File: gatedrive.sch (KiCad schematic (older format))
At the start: 20 parts, among them IC1 HCPL-316J, IC2 IXDD614PI, p1 POWER SUPPLY CONNECTOR., p2 IGBT CONNECTOR., p3 CONTROLLER CONNECTOR.

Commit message: START
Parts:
- p1: value POWER SUPPLY CONNECTOR. -> SMPS CONNECTOR.
- p3: value CONTROLLER CONNECTOR. -> MIC CONNECTOR.
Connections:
- wire segments 48 -> 57
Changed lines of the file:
@@
 P 850 5100
 F 0 "p1" H 850 4900 50  0000 C CNN
-F 1 "POWER SUPPLY CONNECTOR." V 950 5100 39  0000 C CNN
+F 1 "SMPS CONNECTOR." V 950 5100 39  0000 C CNN
 F 2 "Terminal_Blocks:TerminalBlock_Pheonix_MKDS1.5-3pol" H 850 5100 50  0001 C CNN
 F 3 "" H 850 5100 50  0000 C CNN
@@
 P 850 6150
 F 0 "p3" H 850 5850 50  0000 C CNN
-F 1 "CONTROLLER CONNECTOR." V 950 6150 50  0000 C CNN
+F 1 "MIC CONNECTOR." V 950 6150 50  0000 C CNN
 F 2 "Socket_Strips:Socket_Strip_Straight_1x05" H 850 6150 50  0001 C CNN
 F 3 "" H 850 6150 50  0000 C CNN
@@
 a cap to ensure soft turn-off, recommended by datasheet of hcpl.
 Wire Wire Line
-	6950 4950 7500 4950
-Wire Wire Line
-	6250 4950 6650 4950
-Wire Wire Line
-	6250 5050 6250 5150
-Wire Wire Line
-	6250 4750 6250 4850
+	6950 4950 7150 4950
+Wire Wire Line
+	7150 4950 7500 4950
+Wire Wire Line
+	6250 4950 6500 4950
+Wire Wire Line
+	6500 4950 6650 4950
+Wire Wire Line
+	6250 5050 6250 5100
+Wire Wire Line
+	6250 5100 6250 5150
+Wire Wire Line
+	6250 4750 6250 4800
+Wire Wire Line
+	6250 4800 6250 4850
 Connection ~ 6550 4100
 Wire Wire Line
@@
 	6550 4100 6750 4100
 Wire Wire Line
-	6550 4050 6550 4650
+	6550 4050 6550 4100
+Wire Wire Line
+	6550 4100 6550 4650
 Connection ~ 8450 4950
 Wire Wire Line
@@
 Connection ~ 7150 4950
 Wire Wire Line
-	3700 4650 4850 4650
-Wire Wire Line
-	8350 4950 9050 4950
+	3700 4650 4000 4650
+Wire Wire Line
+	4000 4650 4850 4650
+Wire Wire Line
+	8350 4950 8450 4950
+Wire Wire Line
+	8450 4950 8900 4950
+Wire Wire Line
+	8900 4950 9050 4950
 Wire Wire Line
 	9350 4950 9450 4950
 Wire Wire Line
-	9750 4950 10200 4950
+	9750 4950 9950 4950
+Wire Wire Line
+	9950 4950 10200 4950
 Wire Wire Line
 	9700 5250 9950 5250
@@
 Wire Wire Line
 	7050 4100 7200 4100
-Text GLabel 1400 3100 0    60   Input ~ 0
+Text GLabel 1475 3050 0    60   Input ~ 0
 ~RST
 $Comp
 L PWR_FLAG #FLG07
 U 1 1 56C3962F
-P 1400 3100
-F 0 "#FLG07" H 1400 3195 50  0001 C CNN
-F 1 "PWR_FLAG" V 1550 3100 50  0000 C CNN
-F 2 "" H 1400 3100 50  0000 C CNN
-F 3 "" H 1400 3100 50  0000 C CNN
-	1    1400 3100
+P 1475 3050
+F 0 "#FLG07" H 1475 3145 50  0001 C CNN
+F 1 "PWR_FLAG" V 1625 3050 50  0000 C CNN
+F 2 "" H 1475 3050 50  0000 C CNN
+F 3 "" H 1475 3050 50  0000 C CNN
+	1    1475 3050
 	0    1    1    0
 $EndComp

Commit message: cleaning the repo
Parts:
- removed C1, C2, C4, C5: 0.1uF, Capacitors_ThroughHole:C_Disc_D3_P2.5, symbol CP1
- removed C3: 330pF, Capacitors_ThroughHole:C_Disc_D3_P2.5, symbol CP1
- removed C6: 100pF, Capacitors_ThroughHole:C_Disc_D3_P2.5, symbol CP1
- removed C7: 10nF, Capacitors_ThroughHole:C_Disc_D3_P2.5, symbol CP1
- removed D1: RGPO2-20, Diodes_ThroughHole:Diode_DO-41_SOD81_Horizontal_RM10, symbol D
- removed D2: 1N5821, Diodes_ThroughHole:Diode_DO-41_SOD81_Horizontal_RM10, symbol D
- removed IC1: HCPL-316J, Housings_SOIC:SOIC-16_7.5x10.3mm_Pitch1.27mm, symbol HCPL-316J-RESCUE-gatedrive
- removed IC2: IXDD614PI, gatedrive:DIP-8_W7.62mm_LongPads, symbol IXDD614PI-RESCUE-gatedrive
- removed R1: 10K, Capacitors_SMD:C_1206_HandSoldering, symbol R
- removed R2: 25K, Capacitors_SMD:C_1206_HandSoldering, symbol R
- removed R3, R6: 100, Capacitors_SMD:C_1206_HandSoldering, symbol R
- removed R4: 60, Resistors_ThroughHole:Resistor_Horizontal_RM15mm, symbol R
- removed R5: 30ohm ,0.5W, Resistors_ThroughHole:Resistor_Horizontal_RM15mm, symbol R
- removed p1: SMPS CONNECTOR., Terminal_Blocks:TerminalBlock_Pheonix_MKDS1.5-3pol, symbol CONN_01X03
- removed p2: IGBT CONNECTOR., Terminal_Blocks:TerminalBlock_Pheonix_MKDS1.5-3pol, symbol CONN_01X03
- removed p3: MIC CONNECTOR., Socket_Strips:Socket_Strip_Straight_1x05, symbol CONN_01X05
- added D17, D18, D19: LED, LEDs:LED-3MM, symbol LED
- added P1: Mic General Connector, Socket_Strips:Socket_Strip_Angled_1x12, symbol CONN_01X12
- added R49, R50, R51: R, Resistors_SMD:R_1206, symbol R
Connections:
- net labels added: T2, T3, T4, T5, T6, T7, T8
- net labels removed: -5V, 15V, C, COM, G
- wire segments 57 -> 4
- no-connect marks 1 -> 0
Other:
- note added: "Indicators"
- note added: "Non-inverting configiration is used for hcpl.\n"
- note removed: "0.1 uF are bypass caps, the 330 pF is the fault filter cap."
- note removed: "7,15 must be left unconnected.\n"
- note removed: "C is the collector of the IGBT."
- note removed: "COM is the auxiliary emitter of the IGBT."
- note removed: "DESAT resistor and diode."
- note removed: "Fault pull-up resistor."
- note removed: "G is the Gate of the IGBT."
- note removed: "GND1 is the ground of the microcontroller.\n"
- note removed: "I'M USING GLOBAL LABELS INSTEAD OF LOCAL LABELS AS THEY LOOK NEATER, LOL."
- note removed: "LEFT OPEN OR CONNECTED TO THE VCC."
- note removed: "MICSUPP is 5 volt from the vcc of the microcontroller.\n"
- note removed: "Output and Input ports\ngrouped togeather."
- note removed: "Pull-Down resistor recommended by the data sheet, based on vbe=0.6 which I am not so sure of."
- note removed: "T1 is the PWM control signal from the microcontroller."
- note removed: "a cap to ensure soft turn-off, recommended by datasheet of hcpl."
- note removed: "blanking capacitor"
- note removed: "power flags are used to tell the Eeschema program \nwhich pins are driven by powe sources, \nthey have no physical existance.\n"

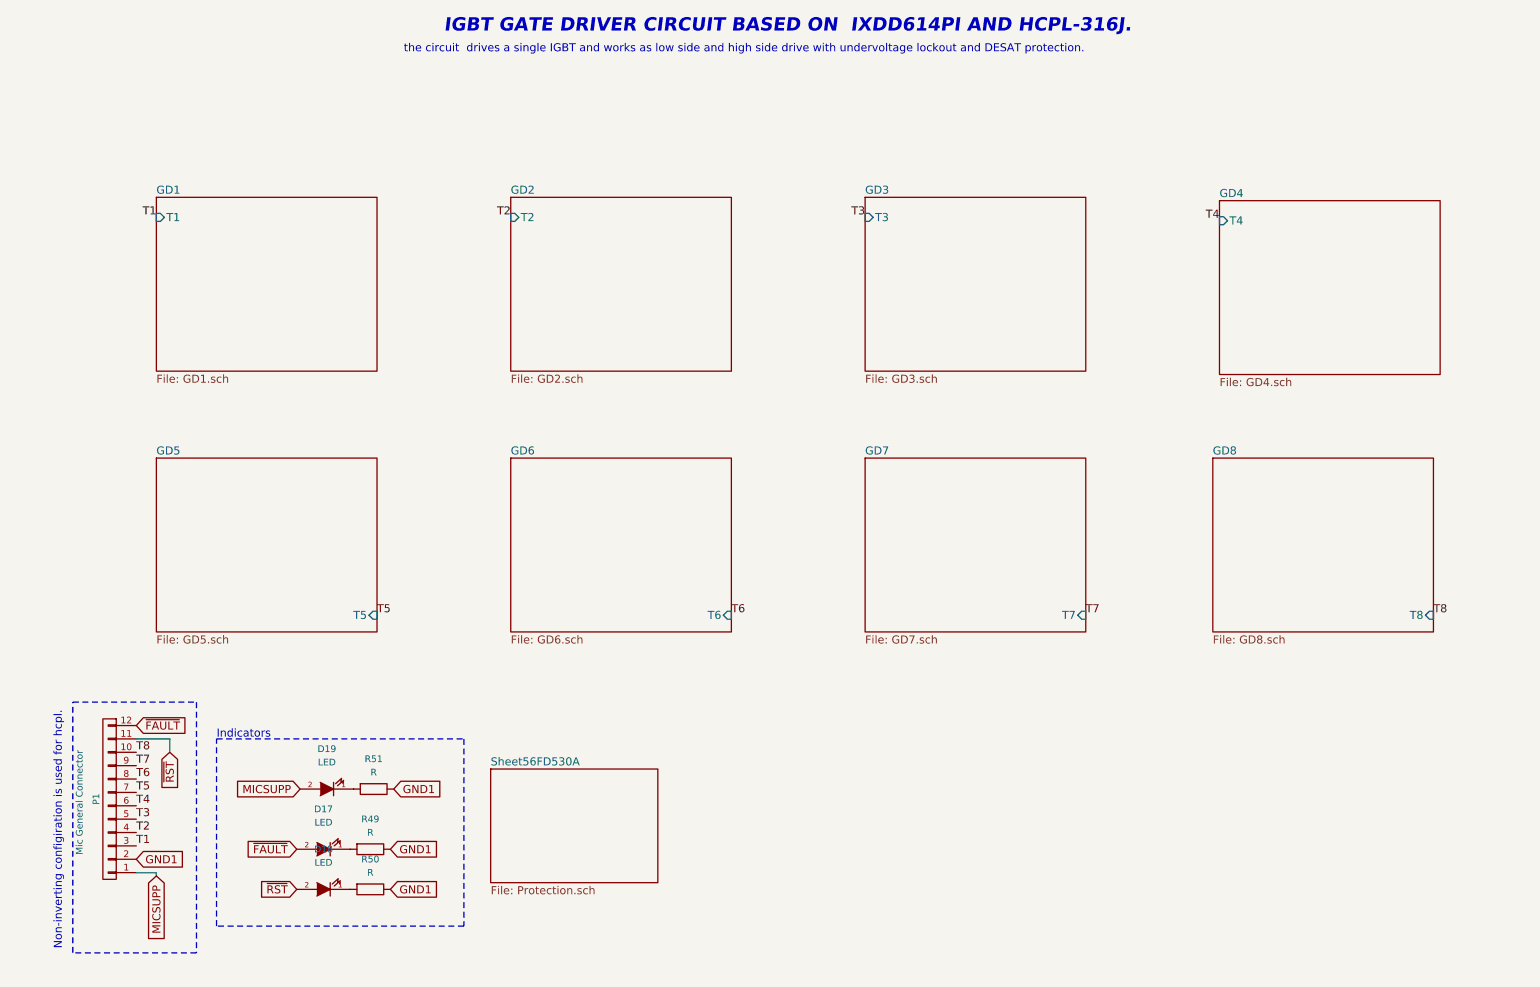
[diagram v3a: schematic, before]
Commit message: cleaning the schematic
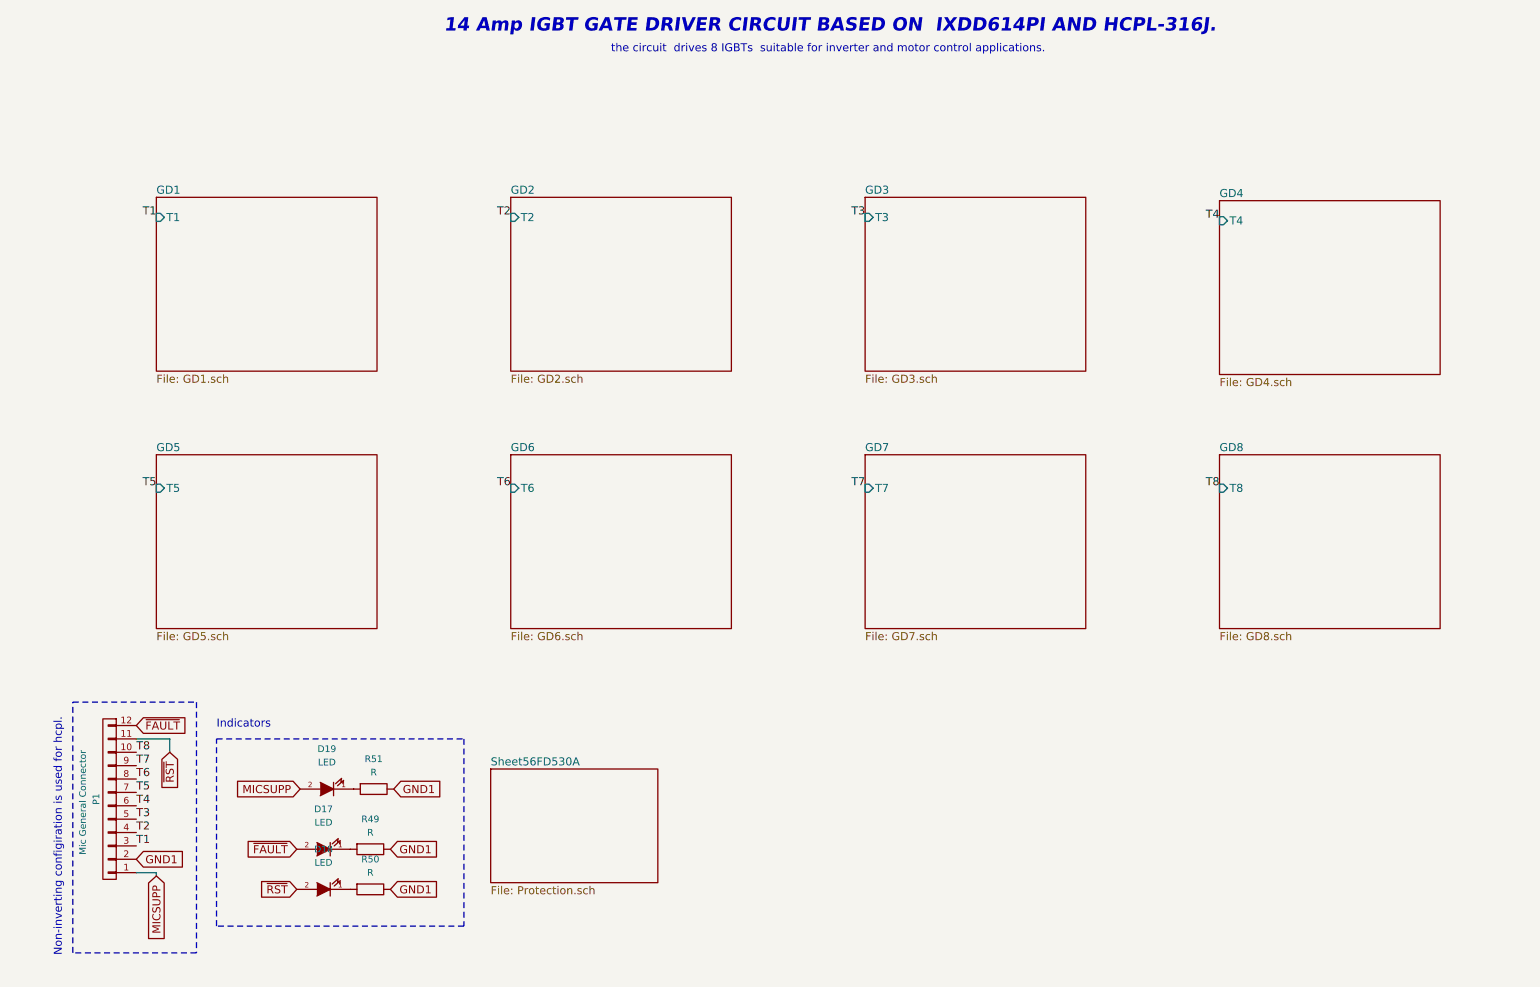
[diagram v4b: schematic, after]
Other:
- note added: "14 Amp IGBT GATE DRIVER CIRCUIT BASED ON IXDD614PI AND HCPL-316J."
- note added: "the circuit drives 8 IGBTs suitable for inverter and motor control applications."
- note removed: "IGBT GATE DRIVER CIRCUIT BASED ON IXDD614PI AND HCPL-316J."
- note removed: "the circuit drives a single IGBT and works as low side and high side drive with undervoltage lockout and DESAT protection.\n"
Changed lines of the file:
@@
 Sheet 1 10
 Title "IGBT GATE DRIVER SCHEMATIC."
-Date "2016-04-04"
+Date "2016-04-13"
 Rev "3"
 Comp "VSD GRADUATION PROJECT."
@@
 $EndDescr
 Text Notes 3500 800  0    100  Italic 20
-IGBT GATE DRIVER CIRCUIT BASED ON  IXDD614PI AND HCPL-316J.
-Text Notes 3200 950  0    60   ~ 0
-the circuit  drives a single IGBT and works as low side and high side drive with undervoltage lockout and DESAT protection.\n
+14 Amp IGBT GATE DRIVER CIRCUIT BASED ON  IXDD614PI AND HCPL-316J.
 $Sheet
 S 1350 2025 1650 1300
@@
 $EndSheet
 $Sheet
-S 6650 3975 1650 1300
+S 6650 3950 1650 1300
 U 56EF0567
 F0 "GD7" 60
 F1 "GD7.sch" 60
-F2 "T7" I R 8300 5150 60
+F2 "T7" I L 6650 4200 60
 $EndSheet
 $Comp
@@
 P 1000 6525
 F 0 "P1" V 1100 6525 50  0000 C CNN
-F 1 "Mic General Connector" V 1225 6550 50  0000 C CNN
+F 1 "Mic General Connector" V 1200 6550 50  0000 C CNN
 F 2 "Socket_Strips:Socket_Strip_Angled_1x12" H 1000 6525 50  0001 C CNN
 F 3 "" H 1000 6525 50  0000 C CNN
@@
 $EndComp
 $Sheet
-S 4000 3975 1650 1300
+S 4000 3950 1650 1300
 U 56EF0565
 F0 "GD6" 60
 F1 "GD6.sch" 60
-F2 "T6" I R 5650 5150 60
-$EndSheet
-$Sheet
-S 1350 3975 1650 1300
+F2 "T6" I L 4000 4200 60
+$EndSheet
+$Sheet
+S 1350 3950 1650 1300
 U 56EF0563
 F0 "GD5" 60
 F1 "GD5.sch" 60
-F2 "T5" I R 3000 5150 60
-$EndSheet
-$Sheet
-S 9250 3975 1650 1300
+F2 "T5" I L 1350 4200 60
+$EndSheet
+$Sheet
+S 9300 3950 1650 1300
 U 56EF0569
 F0 "GD8" 60
 F1 "GD8.sch" 60
-F2 "T8" I R 10900 5150 60
+F2 "T8" I L 9300 4200 60
 $EndSheet
 $Sheet
@@
 Text Label 1200 6175 0    60   ~ 0
 T8
-Text Label 3000 5150 0    60   ~ 0
+Text Label 1350 4200 2    60   ~ 0
 T5
-Text Label 5650 5150 0    60   ~ 0
+Text Label 4000 4200 2    60   ~ 0
 T6
-Text Label 8300 5150 0    60   ~ 0
+Text Label 6650 4200 2    60   ~ 0
 T7
-Text Label 10900 5150 0    60   ~ 0
+Text Label 9300 4200 2    60   ~ 0
 T8
 Text GLabel 1200 5975 2    60   Input ~ 0
@@
 Wire Notes Line
 	1800 7475 1800 6075
-Text Notes 1800 6075 0    60   ~ 0
+Text Notes 1800 6000 0    60   ~ 0
 Indicators
 Wire Notes Line
@@
 F1 "Protection.sch" 60
 $EndSheet
-Text Notes 650  7650 1    60   ~ 0
+Text Notes 650  7700 1    60   ~ 0
 Non-inverting configiration is used for hcpl.\n
+Text Notes 4750 950  0    60   ~ 0
+the circuit  drives 8 IGBTs  suitable for inverter and motor control applications.
 $EndSCHEMATC

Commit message: completion of the layout, initial layout of the protection circuit, reducing number of circuit to 7
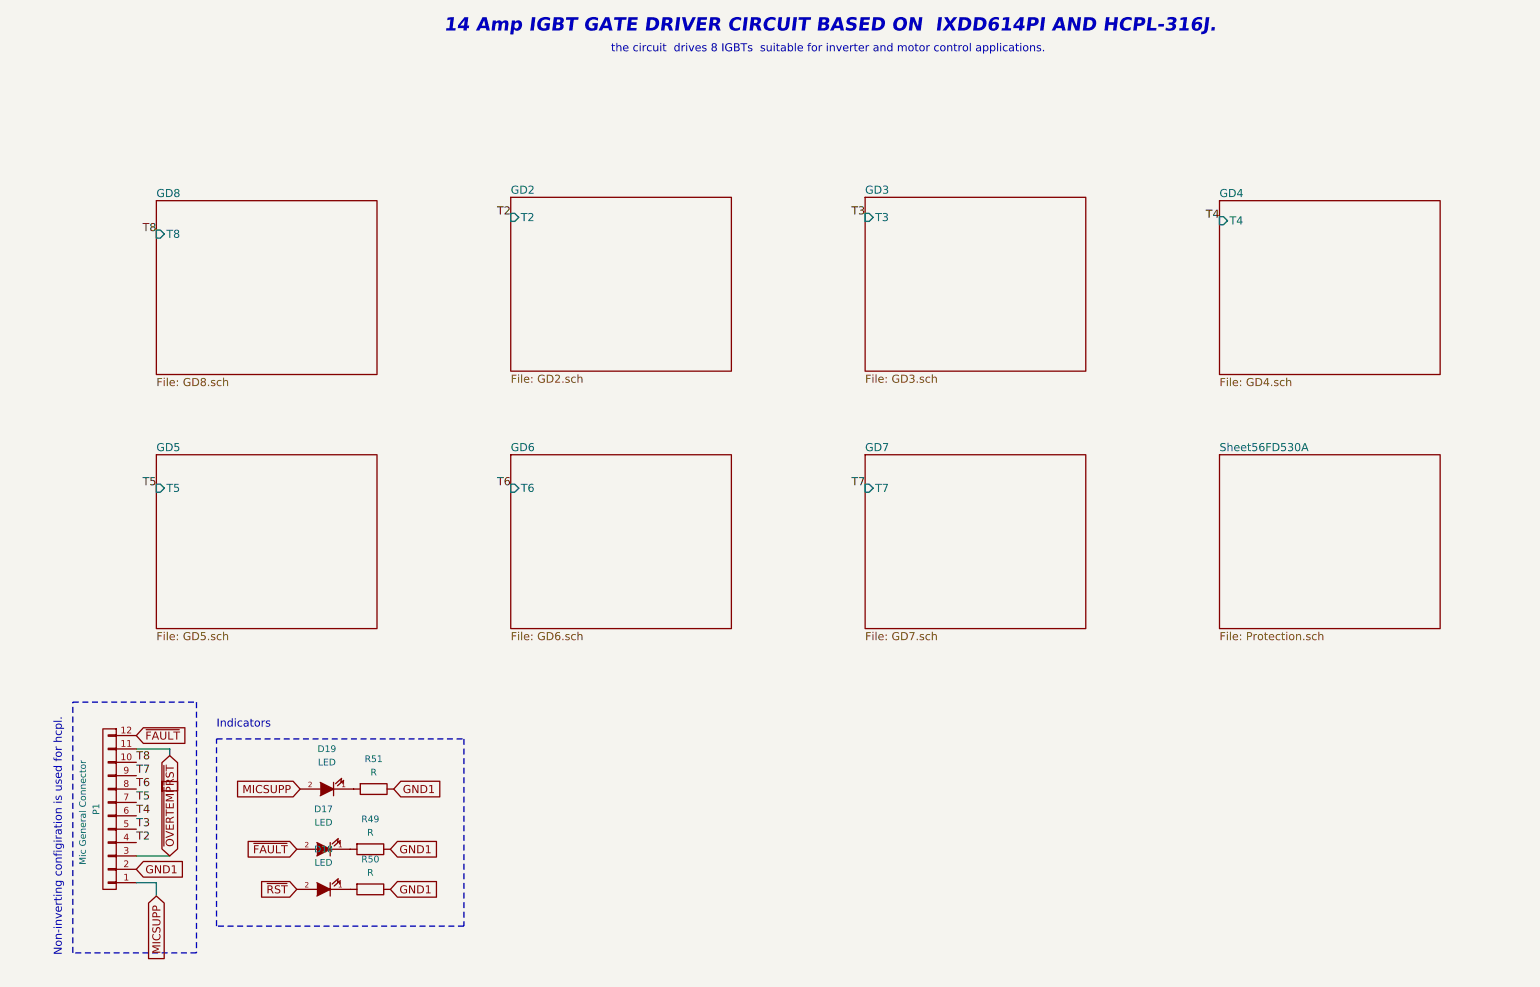
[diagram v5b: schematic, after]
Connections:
- net T1 renamed ~OVERTEMP
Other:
- moved on the sheet: P1
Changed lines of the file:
@@
 EESchema Schematic File Version 2
+LIBS:Symbols_DCDC-ACDC-Converter_RevC_20Jul2012
+LIBS:Symbols_EN60617_13Mar2013
+LIBS:Symbols_EN60617-10_HF-Radio_DRAFT_12Sep2013
+LIBS:Symbols_ICs-Diskrete_RevD10
+LIBS:Symbols_ICs-Opto_RevB_16Sep2013
+LIBS:Symbols_Microcontroller_Philips-NXP_RevA_06Oct2013
+LIBS:SymbolsSimilarEN60617+oldDIN617-RevE8
+LIBS:Symbols_Socket-DIN41612_RevA
+LIBS:Symbols_Transformer-Diskrete_RevA
 LIBS:power
 LIBS:device
@@
 $Descr A4 11693 8268
 encoding utf-8
-Sheet 1 10
+Sheet 1 9
 Title "IGBT GATE DRIVER SCHEMATIC."
 Date "2016-04-13"
@@
 14 Amp IGBT GATE DRIVER CIRCUIT BASED ON  IXDD614PI AND HCPL-316J.
 $Sheet
-S 1350 2025 1650 1300
-U 56EF01DA
-F0 "GD1" 60
-F1 "GD1.sch" 60
-F2 "T1" I L 1350 2175 60
-$EndSheet
-$Sheet
 S 6650 3950 1650 1300
 U 56EF0567
@@
 L CONN_01X12 P1
 U 1 1 56EF0F9E
-P 1000 6525
-F 0 "P1" V 1100 6525 50  0000 C CNN
-F 1 "Mic General Connector" V 1200 6550 50  0000 C CNN
-F 2 "Socket_Strips:Socket_Strip_Angled_1x12" H 1000 6525 50  0001 C CNN
-F 3 "" H 1000 6525 50  0000 C CNN
-	1    1000 6525
+P 1000 6600
+F 0 "P1" V 1100 6600 50  0000 C CNN
+F 1 "Mic General Connector" V 1200 6625 50  0000 C CNN
+F 2 "Socket_Strips:Socket_Strip_Angled_1x12" H 1000 6600 50  0001 C CNN
+F 3 "" H 1000 6600 50  0000 C CNN
+	1    1000 6600
 	-1   0    0    1
 $EndComp
@@
 $EndSheet
 $Sheet
-S 9300 3950 1650 1300
-U 56EF0569
-F0 "GD8" 60
-F1 "GD8.sch" 60
-F2 "T8" I L 9300 4200 60
-$EndSheet
-$Sheet
 S 9300 2050 1650 1300
 U 56EF0560
@@
 F2 "T2" I L 4000 2175 60
 $EndSheet
-Text Label 1350 2175 2    60   ~ 0
-T1
 Text Label 4000 2175 2    60   ~ 0
 T2
@@
 Text Label 9300 2200 2    60   ~ 0
 T4
-Text Label 1200 6875 0    60   ~ 0
-T1
-Text Label 1200 6775 0    60   ~ 0
+Text Label 1200 6850 0    60   ~ 0
 T2
-Text Label 1200 6675 0    60   ~ 0
+Text Label 1200 6750 0    60   ~ 0
 T3
-Text Label 1200 6575 0    60   ~ 0
+Text Label 1200 6650 0    60   ~ 0
 T4
-Text Label 1200 6475 0    60   ~ 0
+Text Label 1200 6550 0    60   ~ 0
 T5
-Text Label 1200 6375 0    60   ~ 0
+Text Label 1200 6450 0    60   ~ 0
 T6
-Text Label 1200 6275 0    60   ~ 0
+Text Label 1200 6350 0    60   ~ 0
 T7
-Text Label 1200 6175 0    60   ~ 0
+Text Label 1200 6250 0    60   ~ 0
 T8
 Text Label 1350 4200 2    60   ~ 0
@@
 Text Label 6650 4200 2    60   ~ 0
 T7
-Text Label 9300 4200 2    60   ~ 0
-T8
-Text GLabel 1200 5975 2    60   Input ~ 0
+Text GLabel 1200 6050 2    60   Input ~ 0
 ~FAULT
-Text GLabel 1450 6175 3    60   Input ~ 0
+Text GLabel 1450 6200 3    60   Input ~ 0
 ~RST
-Wire Wire Line
-	1450 6175 1450 6075
-Wire Wire Line
-	1450 6075 1200 6075
-Text GLabel 1200 6975 2    60   Input ~ 0
+Text GLabel 1200 7050 2    60   Input ~ 0
 GND1
-Text GLabel 1350 7100 3    60   Input ~ 0
+Text GLabel 1350 7250 3    60   Input ~ 0
 MICSUPP
 Wire Wire Line
-	1350 7100 1350 7075
-Wire Wire Line
-	1350 7075 1200 7075
+	1350 7250 1350 7150
+Wire Wire Line
+	1350 7150 1200 7150
 $Comp
 L LED D19
@@
 	725  7675 725  5800
 $Sheet
-S 3850 6300 1250 850
+S 9300 3950 1650 1300
 U 56FD530B
 F0 "Sheet56FD530A" 60
@@
 Text Notes 4750 950  0    60   ~ 0
 the circuit  drives 8 IGBTs  suitable for inverter and motor control applications.
+Text Label 1350 2300 2    60   ~ 0
+T8
+$Sheet
+S 1350 2050 1650 1300
+U 56EF0569
+F0 "GD8" 60
+F1 "GD8.sch" 60
+F2 "T8" I L 1350 2300 60
+$EndSheet
+Text GLabel 1450 6950 1    60   Input ~ 0
+~OVERTEMP
+Wire Wire Line
+	1450 6200 1450 6150
+Wire Wire Line
+	1450 6150 1200 6150
+Wire Wire Line
+	1450 6950 1200 6950
 $EndSCHEMATC
